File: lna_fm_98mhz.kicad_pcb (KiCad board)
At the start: 2 copper layers, 46 x 30 mm, 31 parts, among them J1 SMA_50R_IN, J2 SMA_50R_OUT, J3 BAT_PADS, Q1 MMBT5179

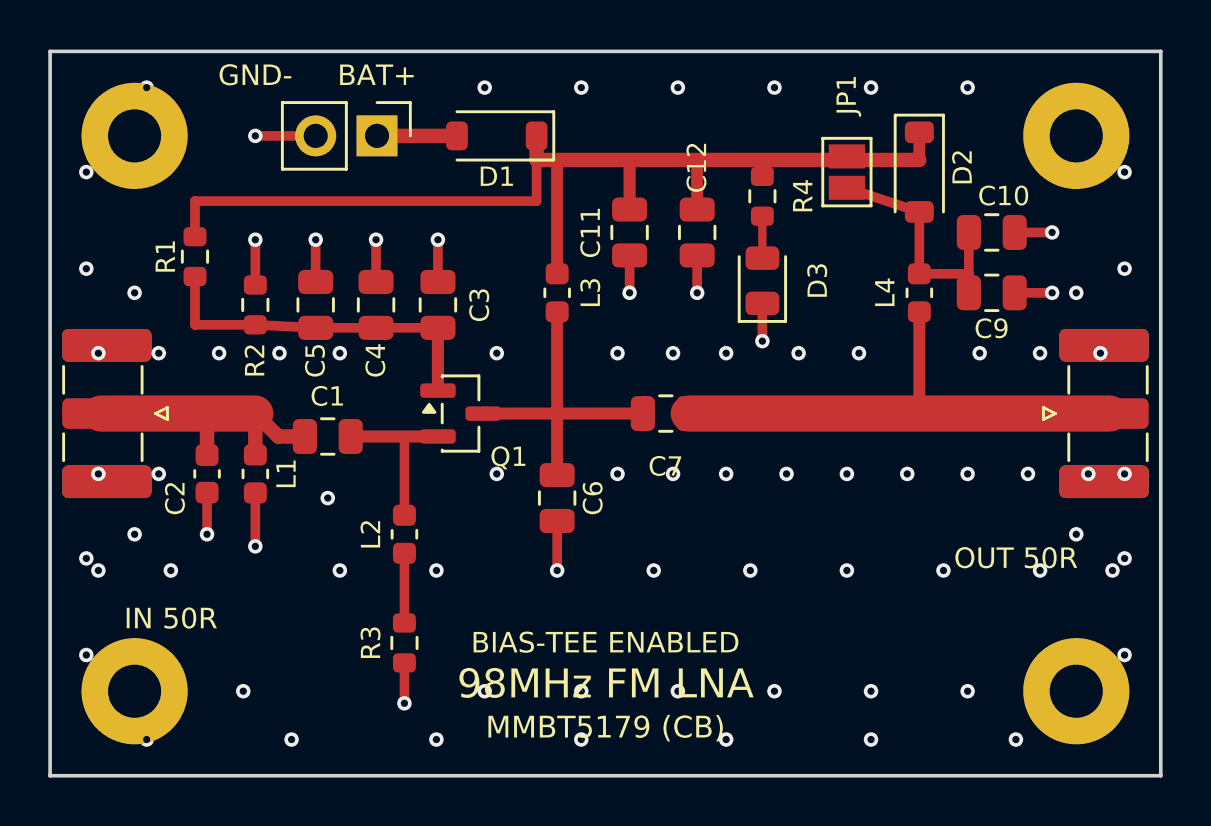
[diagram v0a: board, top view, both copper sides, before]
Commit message: Relocate power header to 20mm and LED to (10mm, 2mm) with 0 DRC violations
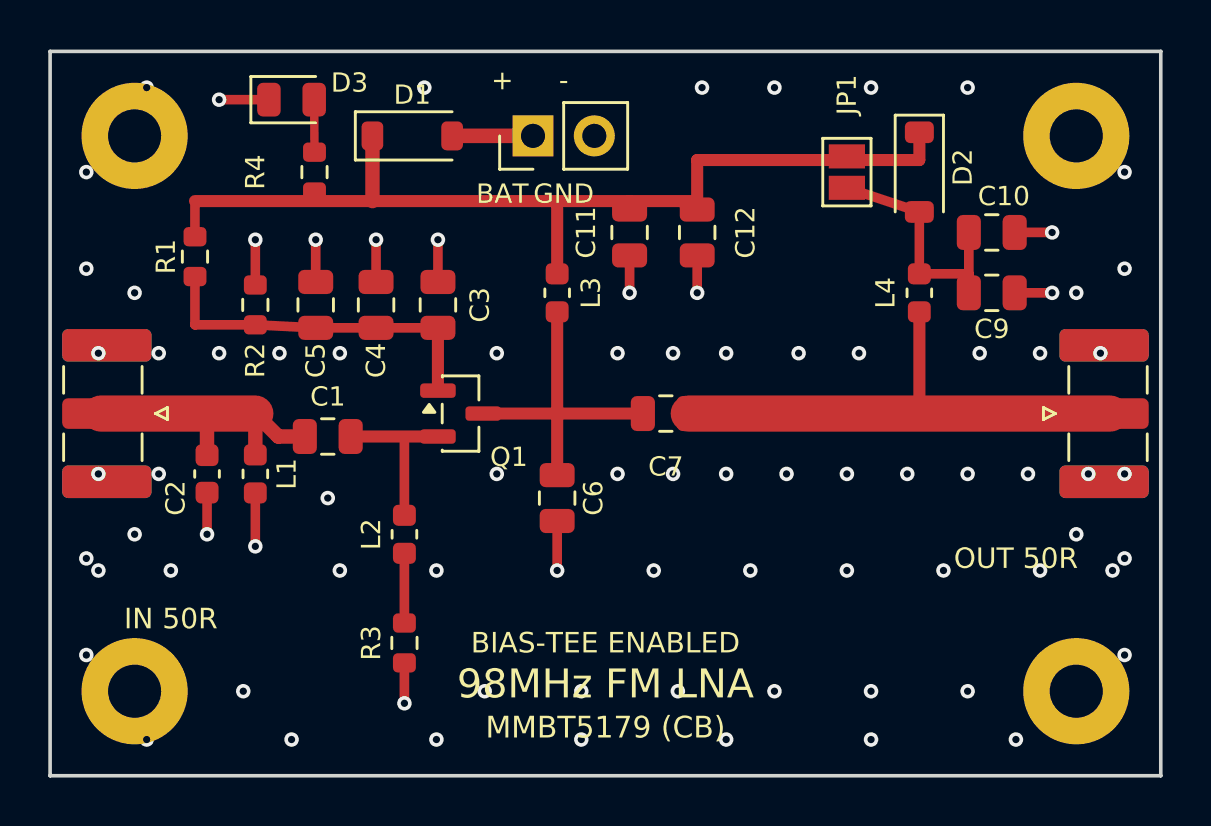
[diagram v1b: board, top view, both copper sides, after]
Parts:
- moved D3 20.9 mm to (10.0, 2.00), turned to 0 degrees
- moved R4 18.6 mm to (10.9, 5.00), turned to 90 degrees
- moved J3 6.46 mm to (20.0, 3.50), turned to 90 degrees
- moved D1 3.50 mm to (15.0, 3.50), turned to 0 degrees
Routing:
- net VCC: track 45.0 -> 41.3 mm
- net GND: track 25.1 -> 23.0 mm, vias 85 -> 83
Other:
- board text added: "+"
- board text added: "-"
- board text added: "BAT"
- board text added: "GND"
- board text removed: "BAT+"
- board text removed: "GND-"

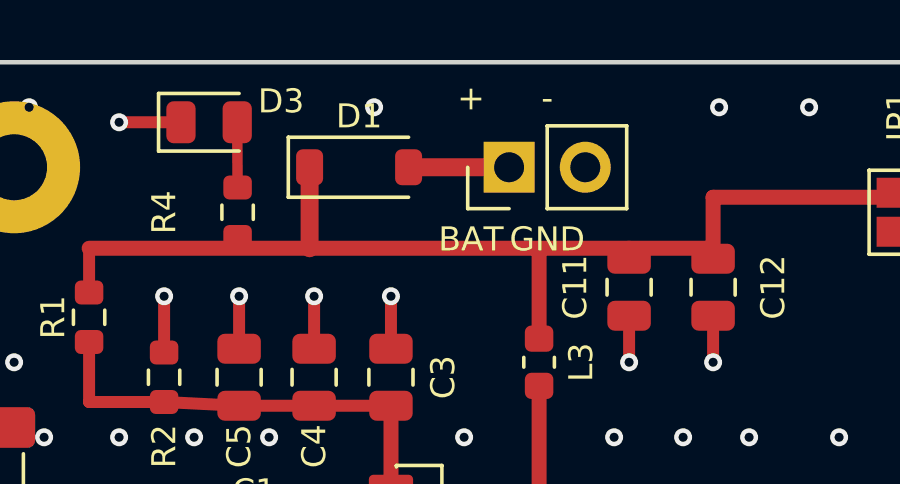
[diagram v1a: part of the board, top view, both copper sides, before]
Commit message: Center power connector at 19mm in 15mm-23mm USB port cutout window
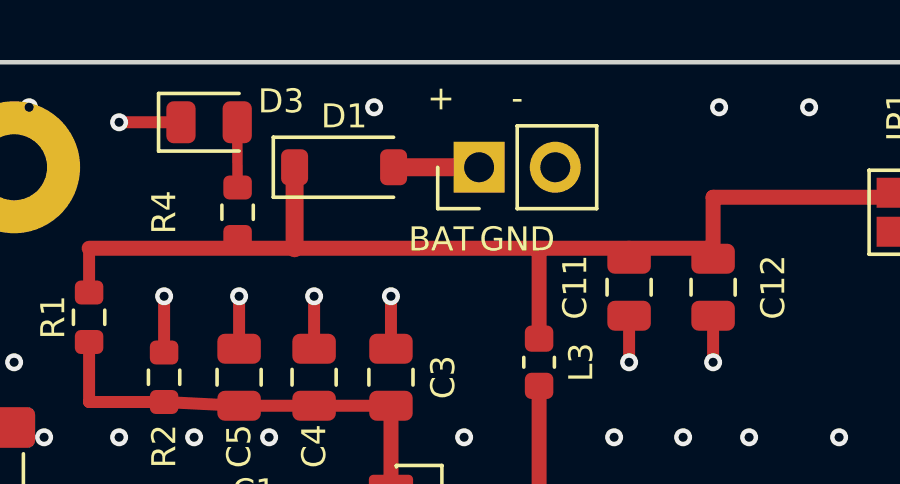
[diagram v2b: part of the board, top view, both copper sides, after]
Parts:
- moved J3 1.00 mm to (19.0, 3.50)
- moved D1 0.50 mm to (14.5, 3.50)
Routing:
- net /BAT_IN: track 3.35 -> 2.85 mm

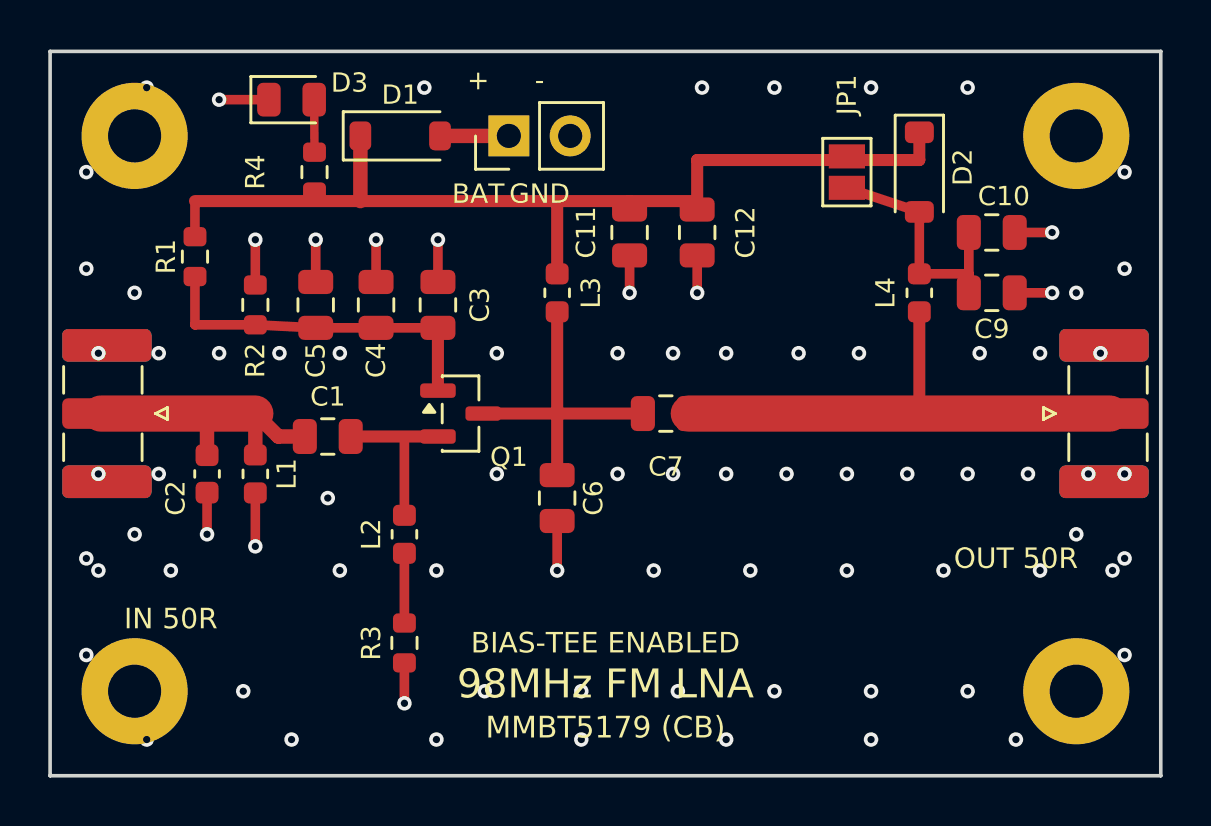
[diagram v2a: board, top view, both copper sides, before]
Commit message: fix(pcb): resize PCB to 34x29mm matching OpenSourceSDRLab enclosure
- Compact PCB outline to 34.00 x 29.00 mm (X: [0, 34], Y: [0, 29])
- Lower symmetrical RF centerline to Y = 14.50 mm
- Set corner M2 mounting holes at (2.5, 2.5), (31.5, 2.5), (2.5, 26.5), (31.5, 26.5) mm
- Re-route CPWG transmission lines, tuned output tank, and bias-tee
- Rotate L4 choke horizontally to eliminate courtyard overlap
- Verify KiCad DRC: 0 errors, 0 warnings, 0 unconnected items
- Regenerate 3D mechanical models (bare board, full assembly, connector-free)
- Re-render 2D photomasks, composite previews, and 3D raytraced renders
- Update production Gerbers, Excellon drill files, and README specifications
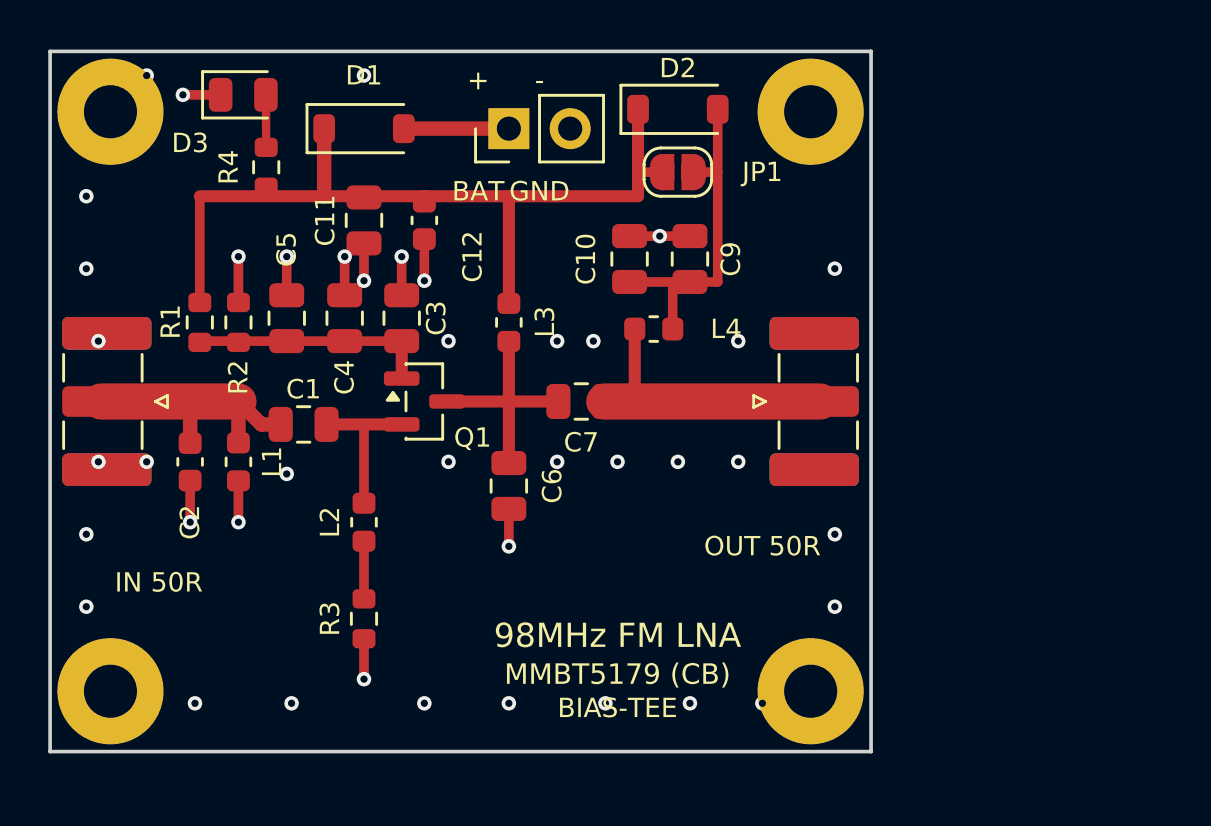
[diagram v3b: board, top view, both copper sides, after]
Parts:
- C12: footprint C_0805_2012Metric -> C_0603_1608Metric
- JP1: value BYPASS -> SolderJumper_Open; footprint SolderJumper-2_P1.3mm_Open_Pad1.0x1.5mm -> SolderJumper-2_P1.3mm_Open_RoundedPad1.0x1.5mm
- moved C10 15.0 mm to (24.0, 8.60), turned to 90 degrees
- moved C9 12.6 mm to (26.5, 8.60), turned to 90 degrees
- moved J2 12.0 mm to (31.9, 14.5)
- moved C12 11.3 mm to (15.5, 7.00)
- moved L4 11.1 mm to (25.0, 11.5), turned to 0 degrees
- moved H2 11.0 mm to (31.5, 2.50)
- moved C11 11.0 mm to (13.0, 7.00)
- moved H4 11.0 mm to (31.5, 26.5)
- moved D2 10.3 mm to (26.0, 2.40), turned to 0 degrees
- moved JP1 7.00 mm to (26.0, 5.00), turned to 180 degrees
- moved C7 3.54 mm to (22.0, 14.5)
- moved R1 2.73 mm to (6.20, 11.2)
- moved L3 2.35 mm to (19.0, 11.2)
- moved C6 2.06 mm to (19.0, 18.0)
- moved D3 2.01 mm to (8.00, 1.80)
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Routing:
- net /RF_OUT_50R: track 21.7 -> 11.9 mm
- net VCC: track 41.3 -> 35.0 mm
- net /BASE: track 14.7 -> 9.91 mm
- net /COLLECTOR: track 13.4 -> 9.65 mm
- net /BIAS_TEE_DC: track 11.1 -> 13.7 mm
- net GND: track 23.0 -> 20.7 mm, vias 83 -> 41
- net /BAT_IN: track 2.85 -> 4.35 mm
- net /RF_IN_50R: track 12.3 -> 11.3 mm
- net Net-(L2-Pad2): track 2.89 -> 2.39 mm
- net /EMITTER: track 6.88 -> 6.38 mm
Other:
- board size 46 x 30 mm -> 34 x 29 mm
- board text added: "BIAS-TEE"
- board text removed: "BIAS-TEE ENABLED"

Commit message: fix(pcb): update PCB outline to 34x29mm with R=3mm curved fillets matching h4m-keytop-24 enclosure
- Redesign Edge.Cuts with 4x R=3.0mm concentric corner fillets matching enclosure posts
- Align M2 mounting holes at (3.0, 3.0), (31.0, 3.0), (3.0, 26.0), (31.0, 26.0) mm
- Set RF centerline to Y = 17.00 mm matching asymmetric enclosure SMA cutouts
- Center DC power / battery header at X = 18.50 mm in the 7.6mm USB enclosure window
- Verify KiCad DRC: 0 errors, 0 warnings, 0 unconnected items (drc_report.json)
- Prove exact zero 3D interference in FreeCAD with h4m-keytop-24.step enclosure
- Re-export 3D deliverables: assembly, bare board, and connector-free STEP & STL models
- Re-run openEMS full-board 3D EM FDTD simulation and regenerate 4-port S-parameters (.s4p)
- Execute QUCS circuit co-simulation and regenerate Smith chart and Cartesian plots
- Re-render all 2D artwork, photomasks, and 3D raytraced views
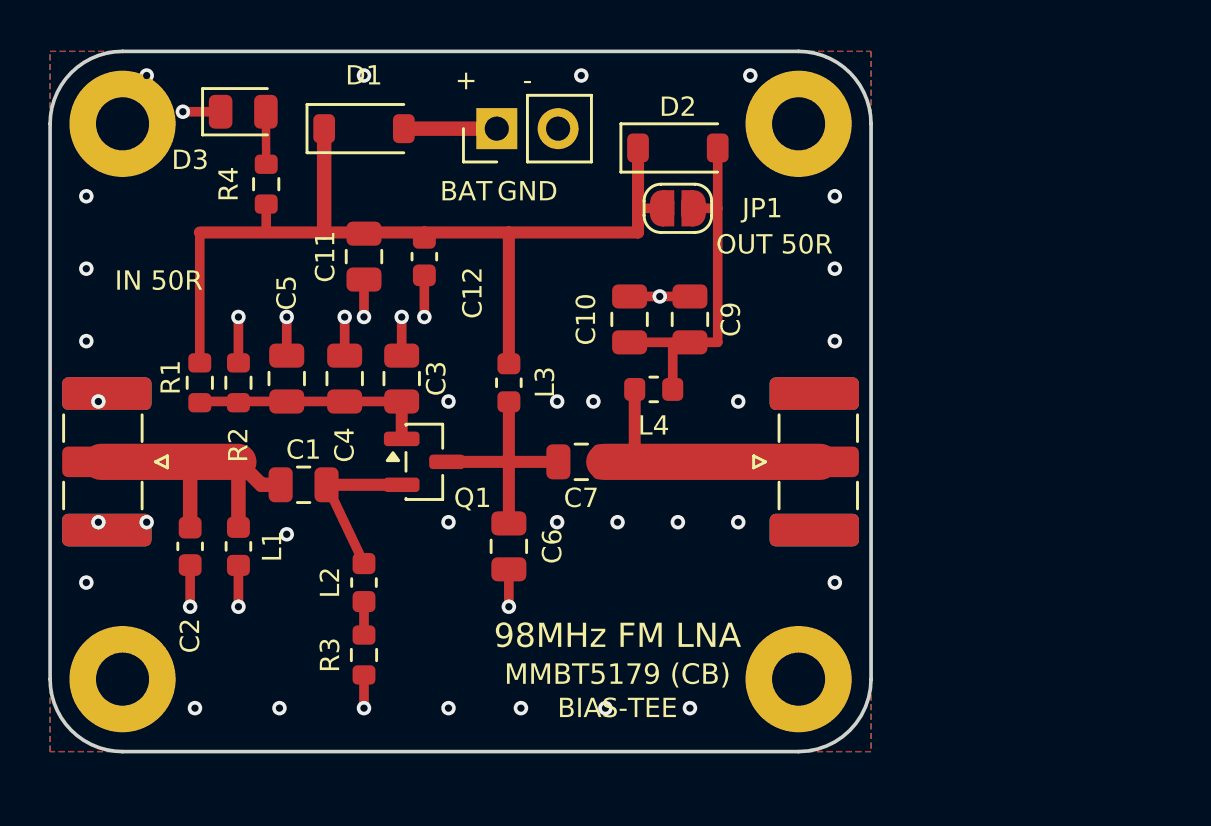
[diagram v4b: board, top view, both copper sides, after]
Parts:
- moved C2 3.50 mm to (5.80, 20.5)
- moved L1 3.50 mm to (7.80, 20.5)
- moved C1 2.50 mm to (10.5, 17.9)
- moved C10 2.50 mm to (24.0, 11.1)
- moved C3 2.50 mm to (14.6, 13.6)
- moved C4 2.50 mm to (12.2, 13.6)
- moved C5 2.50 mm to (9.80, 13.6)
- moved C6 2.50 mm to (19.0, 20.5)
- moved C7 2.50 mm to (22.0, 17.0)
- moved C9 2.50 mm to (26.5, 11.1)
- moved J1 2.50 mm to (2.10, 17.0)
- moved J2 2.50 mm to (31.9, 17.0)
- moved L2 2.50 mm to (13.0, 22.0)
- moved L3 2.50 mm to (19.0, 13.7)
- moved L4 2.50 mm to (25.0, 14.0)
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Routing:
- net VCC: track 35.0 -> 39.2 mm
- net /RF_IN_50R: track 11.3 -> 13.3 mm
- net Net-(L2-Pad2): track 2.39 -> 1.39 mm
- net /BIAS_TEE_DC: track 13.7 -> 14.6 mm
- net /BAT_IN: track 4.35 -> 3.85 mm
- net GND: track 20.7 -> 20.4 mm, vias 41 -> 43
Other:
- outline, holes or cut-outs redrawn
